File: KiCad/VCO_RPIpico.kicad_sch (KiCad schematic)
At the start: 92 parts, among them J1 AudioJack, J2 Power Jack, SW1 LFO1/2, SW2 Select LFO WaveForm, SW3 Fire4, SW4 Fire3, SW5 Fire2, SW6 Fire1, SW7 Shift2/Save, SW8 Shift1 / Select Bank, U2 PT2399, U3 L7805, sw10 sw_led_fire2, sw11 sw_led_fire3, sw12 sw_led_fire4, sw9 sw_led_fire1

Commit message: CAD und eCAD
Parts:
- removed J1: AudioJack, Connector_Audio:Jack_3.5mm_Ledino_KB3SPRS_Horizontal, symbol Connector:AudioJack2
- added J3: AudioJack3_Ground, symbol Connector_Audio:AudioJack3_Ground
- added R30: 10k, Resistor_SMD:R_1206_3216Metric, symbol Device:R
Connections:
- net GND: now also J3.G, J3.S
- net at RV6.2: now also J3.T, R30.2
- new net: J3.R, R30.1

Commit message: KiCad: Supplier added for some parts
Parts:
- J3: Articlecode (none) -> Reichelt: EBS 35
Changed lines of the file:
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@@
+			)
+		)
+		(property "Articlecode" "Reichelt: EBS 35"
+			(at 276.86 49.53 0)
+			(effects
+				(font
+					(size 1.27 1.27)
+				)
+				(hide yes)
 			)
 		)

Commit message: KiCad: Schaltplan angepasst
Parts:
- removed R1: 1k, Resistor_SMD:R_1206_3216Metric, symbol Device:R
- added C24: 220n, Capacitor_SMD:C_1206_3216Metric, symbol Device:C
- C13: value 82nF -> 68nF
- J1: renamed from J3; footprint (none) -> Audiosockets:Jack_3.5mm_Ledino_KB3SPRS_Horizontal
- R19: value 10k -> 4,7k
- RV1: renamed from R15; value 100k -> 10k; footprint Potentiometer_THT:Potentiometer_Alps_RK09K_Single_Vertical -> poti_alps:Potentiometer_Alps_RK09K_Single_Vertical
- RV2: renamed from R14; value 100k -> 10k; footprint Potentiometer_THT:Potentiometer_Alps_RK09K_Single_Vertical -> poti_alps:Potentiometer_Alps_RK09K_Single_Vertical
- RV3: renamed from R13; value 100k -> 10k; footprint Potentiometer_THT:Potentiometer_Alps_RK09K_Single_Vertical -> poti_alps:Potentiometer_Alps_RK09K_Single_Vertical
- RV4, RV5: footprint Potentiometer_THT:Potentiometer_Alps_RK09K_Single_Vertical -> poti_alps:Potentiometer_Alps_RK09K_Single_Vertical
- RV6: value 100k -> 50k; footprint Potentiometer_THT:Potentiometer_Alps_RK09K_Single_Vertical -> poti_alps:Potentiometer_Alps_RK09K_Single_Vertical
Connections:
- net +3V3: now also RV1.3, RV2.3, RV3.3; no longer RV1.1, RV2.1, RV3.1
- net GND: now also RV1.1, RV2.1, RV3.1; no longer RV1.3, RV2.3, RV3.3
- net Wave_out: now also C24.1
- net at A1.7 (GPIO5): now also C24.2

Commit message: KiCad BOM erstellt
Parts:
- removed D12, D16: LED Fire1, LED_SMD:LED_1206_3216Metric, symbol Device:LED
- removed D13, D17: LED Fire2, LED_SMD:LED_1206_3216Metric, symbol Device:LED
- removed D14, D18: LED Fire3, LED_SMD:LED_1206_3216Metric, symbol Device:LED
- removed D15, D19: LED Fire4, LED_SMD:LED_1206_3216Metric, symbol Device:LED
- removed sw10: sw_led_fire2, switches:Multimec Switch THT, symbol eigene_24:switch_led
- removed sw11: sw_led_fire3, switches:Multimec Switch THT, symbol eigene_24:switch_led
- removed sw12: sw_led_fire4, switches:Multimec Switch THT, symbol eigene_24:switch_led
- removed sw9: sw_led_fire1, switches:Multimec Switch THT, symbol eigene_24:switch_led
- A1: Reichelt (none) -> RASP PI PICO H
- C1, C8: Reichelt (none) -> FT-V 100U 16
- C17, C18: Reichelt (none) -> KEM X5R0805 4,7U
- C21, C23: Reichelt (none) -> SMD ELKO 10/16
- C9: Reichelt (none) -> ELN RVS-16V470MU
- D1: value LED LFO2 -> LED LFO2 yel; Reichelt (none) -> 3004Y1D-EHC-B
- D2: value LED LFO1 -> LED LFO1 yel
- D3: value LED Shift1 -> LED Shift1 yel
- D4: value LED Fire1 -> LED Fire1 blu
- D5: value LED Fire2 -> LED Fire2 blu
- D6: value LED Fire3 -> LED Fire3 blu
- D7: value LED Fire4 -> LED Fire4 blu
- D9: value LED Shift2 -> LED Save red
- J1: Reichelt (none) -> EBS 35
- J2: Reichelt (none) -> CLIFF FCR681465
- R20, R21, R26, R28, R29, R30, RV1, RV2, RV3: Reichelt (none) -> RK09K113-LIN10K
- R23, RV4, RV5: Reichelt (none) -> RK09K113-LIN100K
- RV6: Reichelt (none) -> RK09K113-LIN50K
- SW1, SW2, SW7, SW8: Reichelt (none) -> OMR B3F-1002
- SW3, SW4, SW5, SW6: Reichelt (none) -> RAFI 100.502
- U3: Reichelt (none) -> L78M05CDT STM

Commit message: KiCad änderungen
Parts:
- J1: footprint Audiosockets:Jack_3.5mm_Ledino_KB3SPRS_Horizontal -> Connector_Audio:Jack_6.35mm_Neutrik_NMJ6HFD2_Horizontal
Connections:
- net GND: no longer RV4.2
- net at R19.1, RV4.3: now also RV4.2
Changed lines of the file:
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@@
 	)
 	(junction
-		(at 116.84 53.34)
-		(diameter 0)
-		(color 0 0 0 0)
-	)
-	(junction
 		(at 46.99 30.48)
 		(diameter 0)
@@
 	)
 	(junction
+		(at 124.46 52.07)
+		(diameter 0)
+		(color 0 0 0 0)
+	)
+	(junction
 		(at 138.43 139.7)
 		(diameter 0)
@@
 	(wire
 		(pts
+			(xy 124.46 55.88) (xy 124.46 52.07)
+		)
+		(stroke
+			(width 0)
+			(type default)
+		)
+	)
+	(wire
+		(pts
 			(xy 262.89 49.53) (xy 262.89 52.07)
 		)
@@
 	(wire
 		(pts
-			(xy 116.84 55.88) (xy 116.84 53.34)
-		)
-		(stroke
-			(width 0)
-			(type default)
-		)
-	)
-	(wire
-		(pts
 			(xy 184.15 33.02) (xy 184.15 34.29)
 		)
@@
 	(wire
 		(pts
+			(xy 120.65 55.88) (xy 124.46 55.88)
+		)
+		(stroke
+			(width 0)
+			(type default)
+		)
+	)
+	(wire
+		(pts
 			(xy 134.62 63.5) (xy 134.62 64.77)
 		)
@@
 	(wire
 		(pts
-			(xy 120.65 55.88) (xy 116.84 55.88)
-		)
-		(stroke
-			(width 0)
-			(type default)
-		)
-	)
-	(wire
-		(pts
 			(xy 200.66 63.5) (xy 196.85 63.5)
 		)
@@
 	(label "sw_fire3"
 		(at 111.76 134.62 0)
-		(fields_autoplaced yes)
 		(effects
 			(font
@@
 	(label "led_fire2"
 		(at 49.53 147.32 0)
-		(fields_autoplaced yes)
 		(effects
 			(font
@@
 	(label "sw_fire4"
 		(at 111.76 132.08 0)
-		(fields_autoplaced yes)
 		(effects
 			(font
@@
 	(label "sw_fire2"
 		(at 111.76 137.16 0)
-		(fields_autoplaced yes)
 		(effects
 			(font
@@
 	(label "Wave_out"
 		(at 176.53 25.4 180)
-		(fields_autoplaced yes)
 		(effects
 			(font
@@
 	(label "Wave_out"
 		(at 55.88 114.3 180)
-		(fields_autoplaced yes)
 		(effects
 			(font
@@
 	(label "led_fire1"
 		(at 49.53 139.7 0)
-		(fields_autoplaced yes)
 		(effects
 			(font
@@
 	(label "led_fire4"
 		(at 49.53 162.56 0)
-		(fields_autoplaced yes)
 		(effects
 			(font
@@
 	(label "led_fire3"
 		(at 49.53 154.94 0)
-		(fields_autoplaced yes)
 		(effects
 			(font
@@
 			)
 		)
-		(property "Footprint" "Audiosockets:Jack_3.5mm_Ledino_KB3SPRS_Horizontal"
+		(property "Footprint" "Connector_Audio:Jack_6.35mm_Neutrik_NMJ6HFD2_Horizontal"
 			(at 276.86 49.53 0)
 			(effects

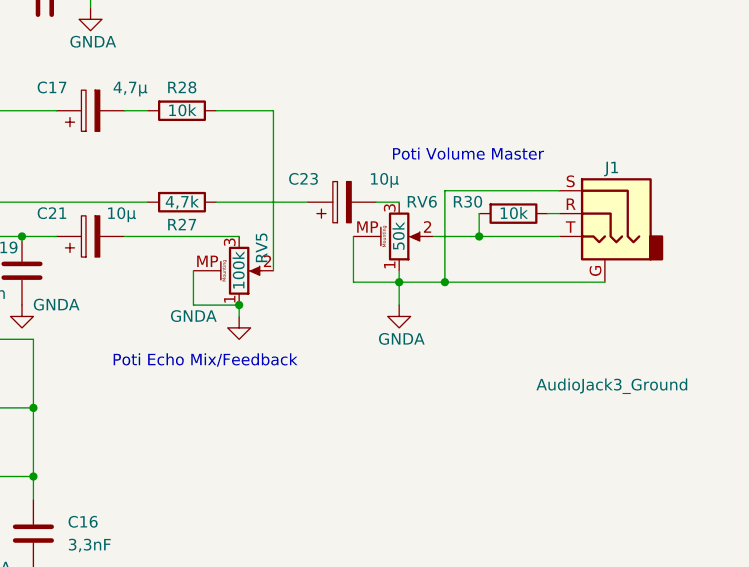
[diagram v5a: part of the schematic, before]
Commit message: PCB correctur
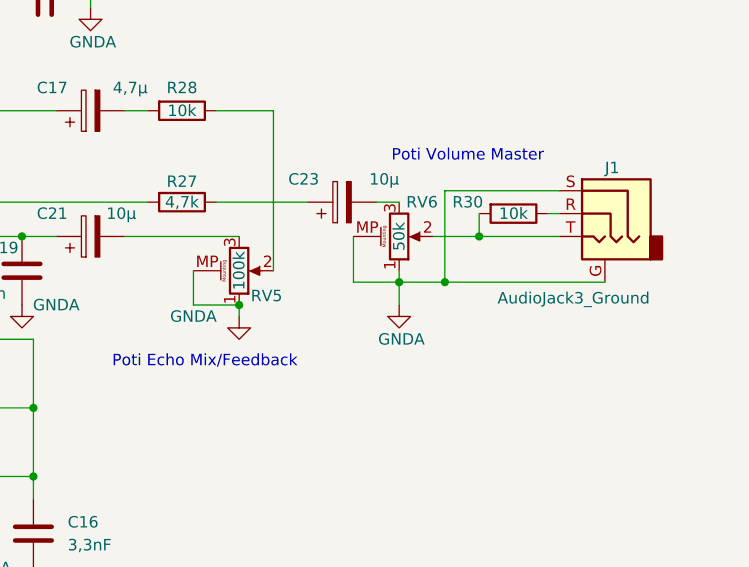
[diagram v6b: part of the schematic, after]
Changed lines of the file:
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@@
 	(label "sw_fire3"
 		(at 111.76 134.62 0)
+		(fields_autoplaced yes)
 		(effects
 			(font
@@
 	(label "led_fire2"
 		(at 49.53 147.32 0)
+		(fields_autoplaced yes)
 		(effects
 			(font
@@
 	(label "sw_fire4"
 		(at 111.76 132.08 0)
+		(fields_autoplaced yes)
 		(effects
 			(font
@@
 	(label "sw_fire2"
 		(at 111.76 137.16 0)
+		(fields_autoplaced yes)
 		(effects
 			(font
@@
 	(label "Wave_out"
 		(at 176.53 25.4 180)
+		(fields_autoplaced yes)
 		(effects
 			(font
@@
 	(label "Wave_out"
 		(at 55.88 114.3 180)
+		(fields_autoplaced yes)
 		(effects
 			(font
@@
 	(label "led_fire1"
 		(at 49.53 139.7 0)
+		(fields_autoplaced yes)
 		(effects
 			(font
@@
 	(label "led_fire4"
 		(at 49.53 162.56 0)
+		(fields_autoplaced yes)
 		(effects
 			(font
@@
 	(label "led_fire3"
 		(at 49.53 154.94 0)
+		(fields_autoplaced yes)
 		(effects
 			(font
@@
 		(dnp no)
 		(property "Reference" "RV5"
-			(at 238.76 53.34 90)
+			(at 239.268 58.674 0)
 			(effects
 				(font
@@
 		)
 		(property "Value" "AudioJack3_Ground"
-			(at 269.24 68.58 0)
+			(at 264.922 58.928 0)
 			(effects
 				(font
@@
 		(dnp no)
 		(property "Reference" "R27"
-			(at 229.87 50.8 90)
+			(at 229.87 45.974 90)
 			(effects
 				(font
